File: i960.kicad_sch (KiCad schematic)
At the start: 52 parts

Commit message: eliminate an inverter by not exposing the 10 and 20mhz clock to the VCC domain
It isn't being used anywhere!
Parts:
- removed C6: (no value), symbol Device:C
- removed unit 6 of U13
- removed unit 5 of U13
- removed U15: (no value), symbol 74xx:74AHC04
- added J?: (no value), symbol Connector_Generic:Conn_01x04
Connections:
- net ME.PF5 is gone; now on net i960.~{DEN}: U16.28 ((AIN15)PF5)
- net ~{RUN_PIC} is gone; now on net ~{CLK_READY}: RN1.7 (R6), U16.15 ((AIN6)PD6)
- net 5V_~{RESET}: now also U14.29 (PF6(~{RESET}))
- net GCM4.HLDA: now also U4.13 (B5)
- net GCM4.HOLD: now also U5.7 (A5)
- net GCM4.USART_PIC_RX: now also U4.14 (B4); no longer U4.13 (B5)
- net PIC.TX: now also U4.6 (A4); no longer U4.7 (A5)
- net i960.CLK: now also J?.2 (Pin_2); no longer U4.9 (A7)
- net i960.CLK2: now also J?.3 (Pin_3); no longer U4.8 (A6)
- net i960.HLDA: now also U4.7 (A5)
- net i960.HOLD: now also U5.13 (B5)
- net i960.~{AS}: now also J?.1 (Pin_1)
- net i960.~{BOOT_SUCCESSFUL}: no longer U14.39 ((XCK0_ALT/SCK)PA6)
- net i960.~{DEN}: no longer U16.33 ((CLKI/TXD0/CCL0-IN0)PA0)
- net GCM4.CLK: no longer names the net of U4.11 (B7)
- net GCM4.CLK2: no longer names the net of U4.12 (B6)
- net PIC.PA7 renamed ~{CLK_READY}
- new net ME.PA0: U16.33 ((CLKI/TXD0/CCL0-IN0)PA0)
- new net PIC.PA6: U14.39 ((XCK0_ALT/SCK)PA6)
- no-connect marks 18 -> 19

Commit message: Drop an AHC74 and two resistor packs
Add an AHC174 in its place. This is for the edge detector. It should now
be far simpler to route this compared to an AHC74
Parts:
- removed C4: (no value), symbol Device:C
- removed RN2, RN3: (no value), symbol Device:R_Network04
- removed U10: (no value), symbol 74xx:74HC74
- added C?: (no value), symbol Device:C
- added U?: (no value), symbol 74xx:74LS174
- gave numbers to parts that had none: 1
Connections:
- net +5V: now also C?.1, U?.16 (VCC); no longer U17.13 (I1d), U17.3 (I1a)
- net EDGE_A: now also U16.9 ((AIN0/CCL2-IN0)PD0), U?.5 (Q1), U?.6 (D2); no longer U16.10 ((AIN1/CCL2-IN1)PD1)
- net EDGE_B: now also U16.10 ((AIN1/CCL2-IN1)PD1), U?.7 (Q2); no longer U16.11 ((AIN2/CCL2-IN2)PD2)
- net GND: now also U17.13 (I1d), U17.3 (I1a), C?.2, U?.8 (GND)
- net PU0: now also RN1.8 (R7)
- net PU1: now also RN1.9 (R8)
- net PU2: now also RN1.10 (R9)
- net PU3: now also RN1.11 (R10)
- net i960.CLK: now also U?.9 (Cp)
- net i960.~{INT0}: now also U13.6; no longer U17.4 (Za)
- net i960.~{INT3}: now also U13.8; no longer U17.12 (Zd)
- net ~{ME_READY}: now also U16.11 ((AIN2/CCL2-IN2)PD2), U?.4 (D1); no longer U16.9 ((AIN0/CCL2-IN0)PD0)
- net at U13.5: now also U17.4 (Za); no longer U14.36 ((XDIR0/SCL/CCL0-OUT)PA3)
- net at U13.9: now also U17.12 (Zd); no longer U14.4 ((XDIR1/~{SS}_ALT/CCL1-OUT)PC3)
- net ~{MR_{0}}: now reaches RN1.12 (R11)
- net ~{MR_{0}}: now also U?.1 (~{Mr})
- net ~{INT0}_OUT renamed INT0_OUT
- net INT0_OUT: now also U14.4 ((XDIR1/~{SS}_ALT/CCL1-OUT)PC3); no longer U13.8
- net ~{INT3}_OUT renamed INT3_OUT
- net INT3_OUT: now also U14.36 ((XDIR0/SCL/CCL0-OUT)PA3); no longer U13.6
- no-connect marks 19 -> 21
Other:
- moved on the sheet: C5, J3, R2, R3, R4, U13C, U13D, U17, U9C

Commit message: Part selection
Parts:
- gave numbers to parts that had none: 2
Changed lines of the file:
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@@
   (symbol (lib_id "power:GND") (at 260.096 182.118 0) (unit 1)
     (in_bom yes) (on_board yes) (fields_autoplaced)
-    (property "Reference" "#PWR?" (id 0) (at 260.096 188.468 0)
+    (property "Reference" "#PWR0103" (id 0) (at 260.096 188.468 0)
       (effects (font (size 1.27 1.27)) hide)
     )
@@
   (symbol (lib_id "74xx:74LS174") (at 260.096 157.988 0) (unit 1)
     (in_bom yes) (on_board yes) (fields_autoplaced)
-    (property "Reference" "U?" (id 0) (at 262.1154 141.5882 0)
+    (property "Reference" "U10" (id 0) (at 262.1154 141.5882 0)
       (effects (font (size 1.27 1.27)) (justify left))
     )
@@
   (symbol (lib_id "Device:C") (at 234.442 176.022 0) (unit 1)
     (in_bom yes) (on_board yes) (fields_autoplaced)
-    (property "Reference" "C?" (id 0) (at 237.363 175.1873 0)
+    (property "Reference" "C4" (id 0) (at 237.363 175.1873 0)
       (effects (font (size 1.27 1.27)) (justify left))
     )
@@
   (symbol (lib_id "power:+5V") (at 260.096 125.73 0) (unit 1)
     (in_bom yes) (on_board yes) (fields_autoplaced)
-    (property "Reference" "#PWR?" (id 0) (at 260.096 129.54 0)
-      (effects (font (size 1.27 1.27)) hide)
-    )
+    (property "Reference" "#PWR0101" (id 0) (at 260.096 129.54 0)
+      (effects (font (size 1.27 1.27)) hide)
+    )

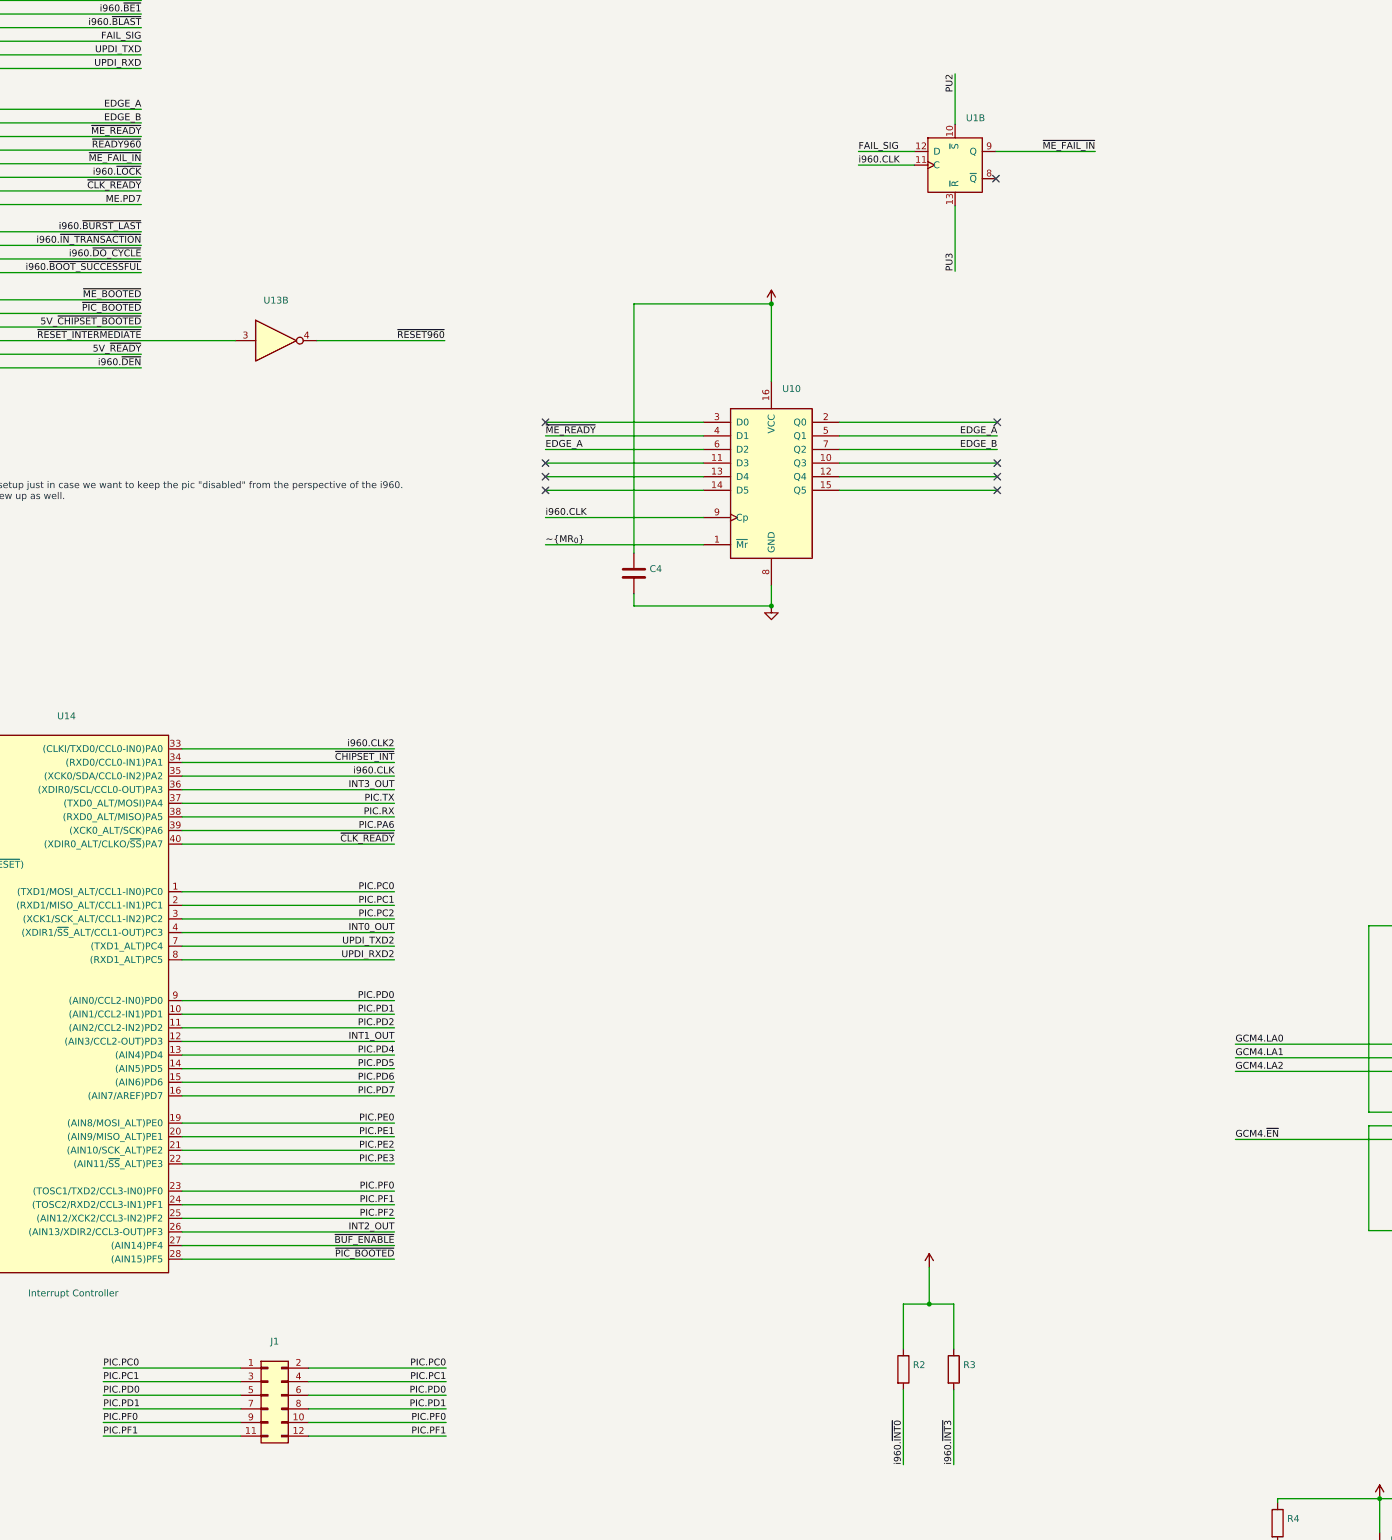
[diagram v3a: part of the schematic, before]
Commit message: Added feather interrupts as well
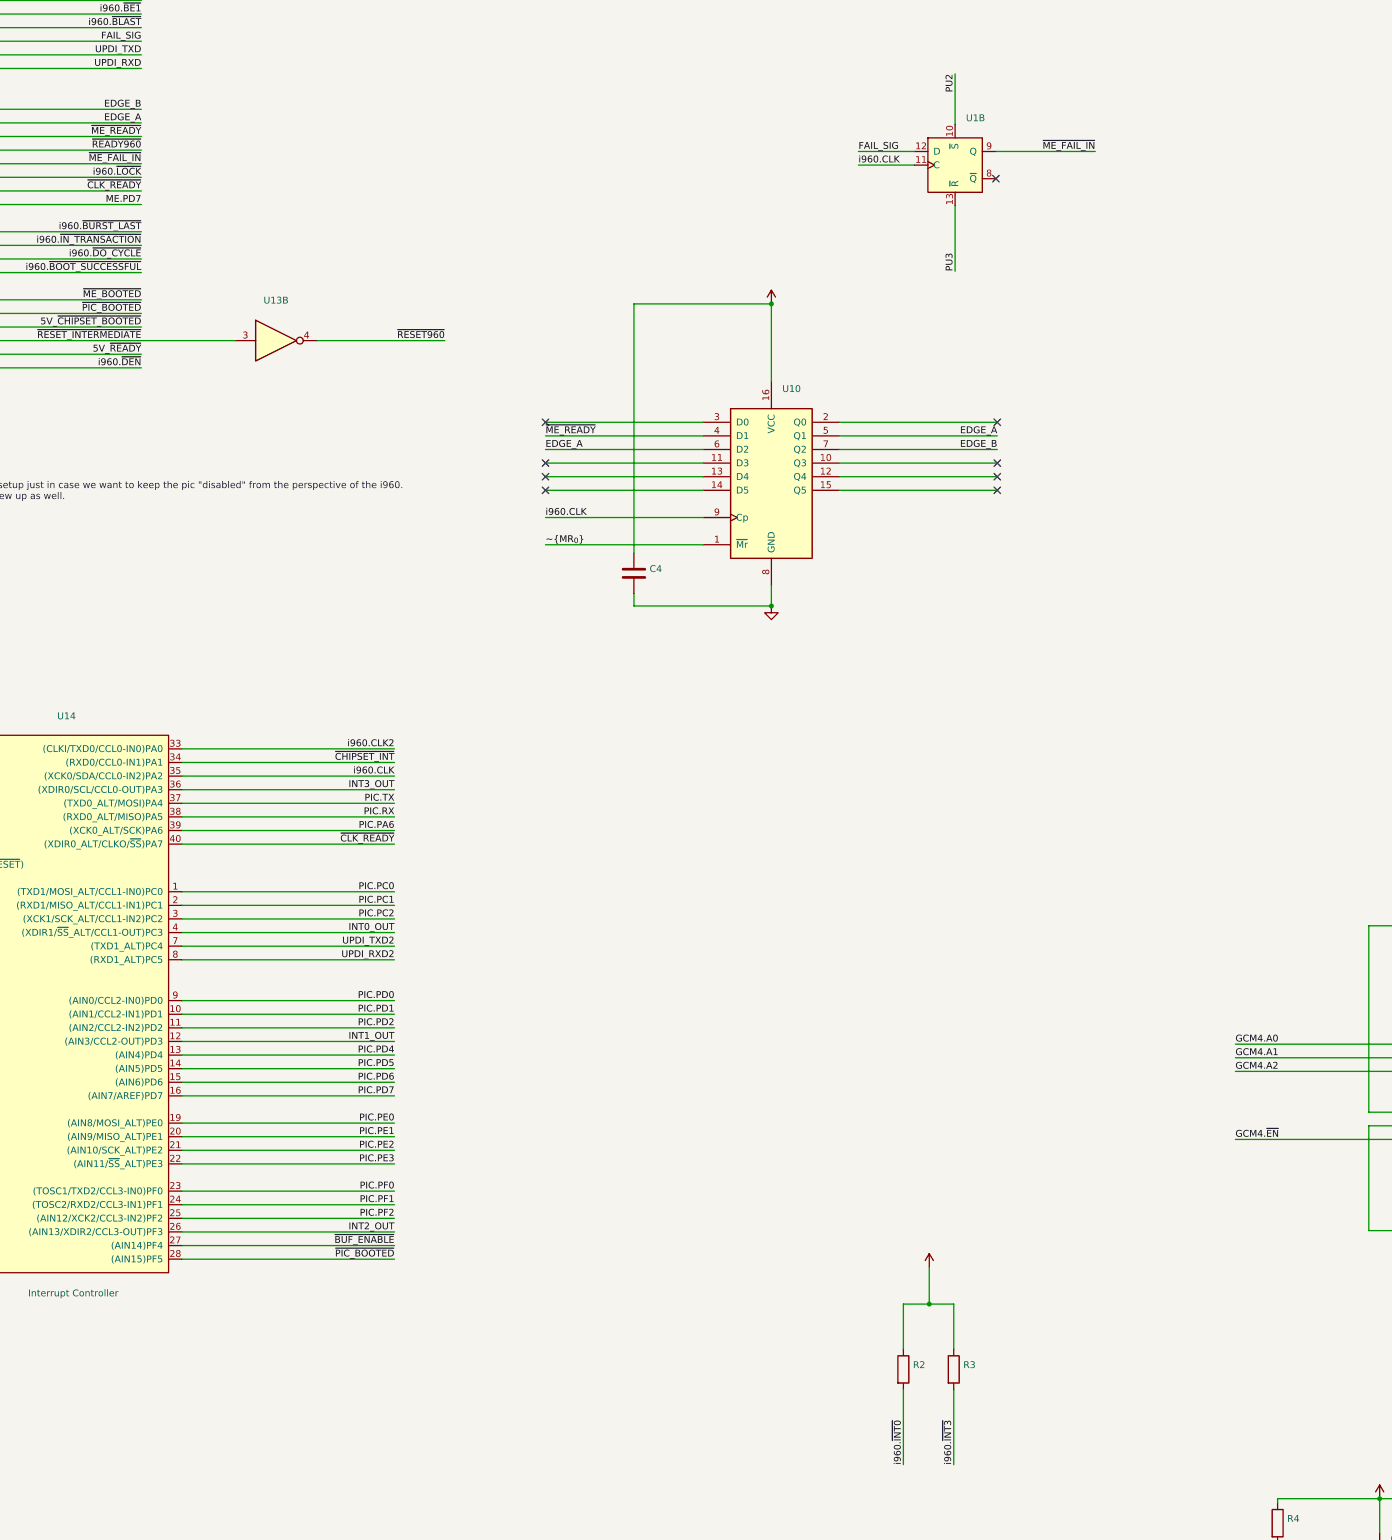
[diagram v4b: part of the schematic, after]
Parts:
- removed J1: (no value), symbol Connector_Generic:Conn_02x06_Odd_Even
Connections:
- net EDGE_A: now also U16.10 ((AIN1/CCL2-IN1)PD1); no longer U16.9 ((AIN0/CCL2-IN0)PD0)
- net EDGE_B: now also U16.9 ((AIN0/CCL2-IN0)PD0); no longer U16.10 ((AIN1/CCL2-IN1)PD1)
- net GCM4.LA0 renamed GCM4.A0
- net GCM4.LA1 renamed GCM4.A1
- net GCM4.LA2 renamed GCM4.A2
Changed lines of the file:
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@@
     (company "Joshua Scoggins")
   )
+  (bus_alias "CHIPSET" (members "~{BURST_LAST}" "~{IN_TRANSACTION}" "~{DO_CYCLE}" "~{BOOT_SUCCESSFUL}" "HLDA" "HOLD" "~{CHIPSET_BOOTED}" "~{RESET960}" "~{READY}" "~{INTR0}" "L[0..7]" "A[0..2]" "USART_ME_TX" "USART_ME_RX" "USART_PIC_TX" "USART_PIC_RX" "D[0..15]" "~{FEATHER_INT[0..1]}"))
   (bus_alias "ADR960" (members "A[0..31]" "D[0..15]" "BURST_A[1..3]" "~{DEN}" "DT\\~{R}" "W\\~{R}" "~{BE[0..1]}" "CLK2" "CLK"))
-  (bus_alias "CHIPSET" (members "~{BURST_LAST}" "~{IN_TRANSACTION}" "~{DO_CYCLE}" "~{BOOT_SUCCESSFUL}" "HLDA" "HOLD" "~{CHIPSET_BOOTED}" "~{RESET960}" "~{READY}" "~{INTR0}" "L[0..7]" "A[0..2]" "USART_ME_TX" "USART_ME_RX" "USART_PIC_TX" "USART_PIC_RX" "D[0..15]"))
   (junction (at 390.398 241.808) (diameter 0) (color 0 0 0 0)
   )
@@
     (stroke (width 0) (type default) (color 0 0 0 0))
   )
-  (wire (pts (xy 135.382 326.898) (xy 161.036 326.898))
-    (stroke (width 0) (type default) (color 0 0 0 0))
-  )
   (wire (pts (xy 386.334 377.952) (xy 414.02 377.952))
     (stroke (width 0) (type default) (color 0 0 0 0))
@@
     (stroke (width 0) (type default) (color 0 0 0 0))
   )
-  (wire (pts (xy 135.382 337.058) (xy 161.036 337.058))
-    (stroke (width 0) (type default) (color 0 0 0 0))
-  )
   (bus (pts (xy 473.202 137.414) (xy 473.202 139.954))
     (stroke (width 0) (type default) (color 0 0 0 0))
@@
     (stroke (width 0) (type default) (color 0 0 0 0))
   )
-  (wire (pts (xy 135.382 329.438) (xy 161.036 329.438))
-    (stroke (width 0) (type default) (color 0 0 0 0))
-  )
   (wire (pts (xy 102.87 127.508) (xy 142.494 127.508))
     (stroke (width 0) (type default) (color 0 0 0 0))
@@
     (stroke (width 0) (type default) (color 0 0 0 0))
   )
-  (wire (pts (xy 135.382 334.518) (xy 161.036 334.518))
-    (stroke (width 0) (type default) (color 0 0 0 0))
-  )
   (wire (pts (xy 65.278 506.222) (xy 65.278 513.334))
     (stroke (width 0) (type default) (color 0 0 0 0))
@@
     (stroke (width 0) (type default) (color 0 0 0 0))
   )
-  (wire (pts (xy 199.39 324.358) (xy 173.736 324.358))
-    (stroke (width 0) (type default) (color 0 0 0 0))
-  )
   (wire (pts (xy 243.078 474.98) (xy 227.076 474.98))
     (stroke (width 0) (type default) (color 0 0 0 0))
@@
     (stroke (width 0) (type default) (color 0 0 0 0))
   )
-  (wire (pts (xy 199.39 326.898) (xy 173.736 326.898))
-    (stroke (width 0) (type default) (color 0 0 0 0))
-  )
   (wire (pts (xy 231.394 49.53) (xy 231.394 31.496))
     (stroke (width 0) (type default) (color 0 0 0 0))
@@
     (stroke (width 0) (type default) (color 0 0 0 0))
   )
-  (wire (pts (xy 199.39 329.438) (xy 173.736 329.438))
-    (stroke (width 0) (type default) (color 0 0 0 0))
-  )
   (wire (pts (xy 467.106 59.944) (xy 502.92 59.944))
     (stroke (width 0) (type default) (color 0 0 0 0))
@@
     (stroke (width 0) (type default) (color 0 0 0 0))
   )
-  (wire (pts (xy 199.39 337.058) (xy 173.736 337.058))
-    (stroke (width 0) (type default) (color 0 0 0 0))
-  )
   (wire (pts (xy 35.052 137.668) (xy 35.052 142.748))
     (stroke (width 0) (type default) (color 0 0 0 0))
@@
     (stroke (width 0) (type default) (color 0 0 0 0))
   )
-  (wire (pts (xy 135.382 331.978) (xy 161.036 331.978))
-    (stroke (width 0) (type default) (color 0 0 0 0))
-  )
   (wire (pts (xy 454.406 23.622) (xy 476.504 23.622))
     (stroke (width 0) (type default) (color 0 0 0 0))
@@
     (stroke (width 0) (type default) (color 0 0 0 0))
   )
-  (wire (pts (xy 199.39 334.518) (xy 173.736 334.518))
-    (stroke (width 0) (type default) (color 0 0 0 0))
-  )
   (wire (pts (xy 217.932 157.988) (xy 247.396 157.988))
     (stroke (width 0) (type default) (color 0 0 0 0))
@@
     (stroke (width 0) (type default) (color 0 0 0 0))
   )
-  (wire (pts (xy 199.39 331.978) (xy 173.736 331.978))
-    (stroke (width 0) (type default) (color 0 0 0 0))
-  )
   (bus (pts (xy 512.064 67.564) (xy 512.064 70.104))
     (stroke (width 0) (type default) (color 0 0 0 0))
@@
     (stroke (width 0) (type default) (color 0 0 0 0))
   )
-  (wire (pts (xy 135.382 324.358) (xy 161.036 324.358))
-    (stroke (width 0) (type default) (color 0 0 0 0))
-  )
   (wire (pts (xy 190.754 452.628) (xy 214.376 452.628))
     (stroke (width 0) (type default) (color 0 0 0 0))
@@
     (effects (font (size 1.27 1.27)) (justify right bottom))
   )
-  (label "GCM4.LA1" (at 346.71 266.446 0)
+  (label "GCM4.A1" (at 346.71 266.446 0)
     (effects (font (size 1.27 1.27)) (justify left bottom))
   )
@@
     (effects (font (size 1.27 1.27)) (justify left bottom))
   )
-  (label "PIC.PF0" (at 199.39 334.518 180)
-    (effects (font (size 1.27 1.27)) (justify right bottom))
-  )
-  (label "PIC.PC1" (at 135.382 326.898 0)
-    (effects (font (size 1.27 1.27)) (justify left bottom))
-  )
   (label "i960.A23" (at 515.874 77.724 0)
     (effects (font (size 1.27 1.27)) (justify left bottom))
@@
     (effects (font (size 1.27 1.27)) (justify left bottom))
   )
-  (label "PIC.PD0" (at 135.382 329.438 0)
-    (effects (font (size 1.27 1.27)) (justify left bottom))
-  )
   (label "PIC.PF2" (at 189.738 296.418 180)
     (effects (font (size 1.27 1.27)) (justify right bottom))
@@
     (effects (font (size 1.27 1.27)) (justify left bottom))
   )
-  (label "PIC.PF1" (at 199.39 337.058 180)
-    (effects (font (size 1.27 1.27)) (justify right bottom))
-  )
   (label "PIC.PA6" (at 189.738 224.028 180)
     (effects (font (size 1.27 1.27)) (justify right bottom))
@@
     (effects (font (size 1.27 1.27)) (justify left bottom))
   )
-  (label "GCM4.LA0" (at 346.71 263.906 0)
+  (label "GCM4.A0" (at 346.71 263.906 0)
     (effects (font (size 1.27 1.27)) (justify left bottom))
   )
@@
     (effects (font (size 1.27 1.27)) (justify right bottom))
   )
-  (label "EDGE_B" (at 142.494 91.948 180)
+  (label "EDGE_B" (at 142.494 89.408 180)
     (effects (font (size 1.27 1.27)) (justify right bottom))
   )
@@
     (effects (font (size 1.27 1.27)) (justify right bottom))
   )
-  (label "PIC.PD1" (at 199.39 331.978 180)
-    (effects (font (size 1.27 1.27)) (justify right bottom))
-  )
   (label "GCM4.L2" (at 502.92 47.244 180)
     (effects (font (size 1.27 1.27)) (justify right bottom))
@@
     (effects (font (size 1.27 1.27)) (justify right bottom))
   )
-  (label "PIC.PD1" (at 135.382 331.978 0)
-    (effects (font (size 1.27 1.27)) (justify left bottom))
-  )
   (label "i960.CLK2" (at 514.604 28.448 0)
     (effects (font (size 1.27 1.27)) (justify left bottom))
@@
     (effects (font (size 1.27 1.27)) (justify right bottom))
   )
-  (label "PIC.PC0" (at 199.39 324.358 180)
-    (effects (font (size 1.27 1.27)) (justify right bottom))
-  )
   (label "i960.A18" (at 515.874 65.024 0)
     (effects (font (size 1.27 1.27)) (justify left bottom))
@@
     (effects (font (size 1.27 1.27)) (justify right bottom))
   )
-  (label "PIC.PD0" (at 199.39 329.438 180)
-    (effects (font (size 1.27 1.27)) (justify right bottom))
-  )
   (label "GCM4.~{BOOT_SUCCESSFUL}" (at 263.398 447.548 180)
     (effects (font (size 1.27 1.27)) (justify right bottom))
@@
     (effects (font (size 1.27 1.27)) (justify left bottom))
   )
-  (label "PIC.PF0" (at 135.382 334.518 0)
-    (effects (font (size 1.27 1.27)) (justify left bottom))
-  )
   (label "INT2_OUT" (at 341.122 377.952 0)
     (effects (font (size 1.27 1.27)) (justify left bottom))
@@
     (effects (font (size 1.27 1.27)) (justify left bottom))
   )
-  (label "PIC.PF1" (at 135.382 337.058 0)
-    (effects (font (size 1.27 1.27)) (justify left bottom))
-  )
   (label "AD14" (at 380.492 188.976 0)
     (effects (font (size 1.27 1.27)) (justify left bottom))
@@
     (effects (font (size 1.27 1.27)) (justify right bottom))
   )
-  (label "GCM4.LA2" (at 346.71 268.986 0)
-    (effects (font (size 1.27 1.27)) (justify left bottom))
-  )
-  (label "PIC.PC0" (at 135.382 324.358 0)
+  (label "GCM4.A2" (at 346.71 268.986 0)
     (effects (font (size 1.27 1.27)) (justify left bottom))
   )
@@
     (effects (font (size 1.27 1.27)) (justify left bottom))
   )
-  (label "PIC.PC1" (at 199.39 326.898 180)
-    (effects (font (size 1.27 1.27)) (justify right bottom))
-  )
   (label "5V_~{CHIPSET_BOOTED}" (at 142.494 130.048 180)
     (effects (font (size 1.27 1.27)) (justify right bottom))
@@
     (effects (font (size 1.27 1.27)) (justify left bottom))
   )
-  (label "EDGE_A" (at 142.494 89.408 180)
+  (label "EDGE_A" (at 142.494 91.948 180)
     (effects (font (size 1.27 1.27)) (justify right bottom))
   )
@@
     (pin "2")
   )
-  (symbol (lib_id "Connector_Generic:Conn_02x06_Odd_Even") (at 166.116 329.438 0) (unit 1)
-    (in_bom yes) (on_board yes) (fields_autoplaced)
-    (property "Reference" "J1" (id 0) (at 167.386 319.3882 0))
-    (property "Value" "" (id 1) (at 167.386 321.9251 0))
-    (property "Footprint" "" (id 2) (at 166.116 329.438 0)
-      (effects (font (size 1.27 1.27)) hide)
-    )
-    (property "Datasheet" "~" (id 3) (at 166.116 329.438 0)
-      (effects (font (size 1.27 1.27)) hide)
-    )
-    (pin "1")
-    (pin "10")
-    (pin "11")
-    (pin "12")
-    (pin "2")
-    (pin "3")
-    (pin "4")
-    (pin "5")
-    (pin "6")
-    (pin "7")
-    (pin "8")
-    (pin "9")
-  )
   (symbol (lib_id "power:GND") (at 161.036 531.622 0) (unit 1)
